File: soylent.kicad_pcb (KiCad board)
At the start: 2 copper layers, 34.5 x 43.2 mm, 23 parts, among them J1 DB9_Female, J2 Conn_01x04, J3 Conn_01x04, J4 Conn_02x03_Counter_Clockwise, Q1 BC847BPN, Q2 BC847BPN, U1 ATtiny202-SS, U2 MIC5504-3.3YM5

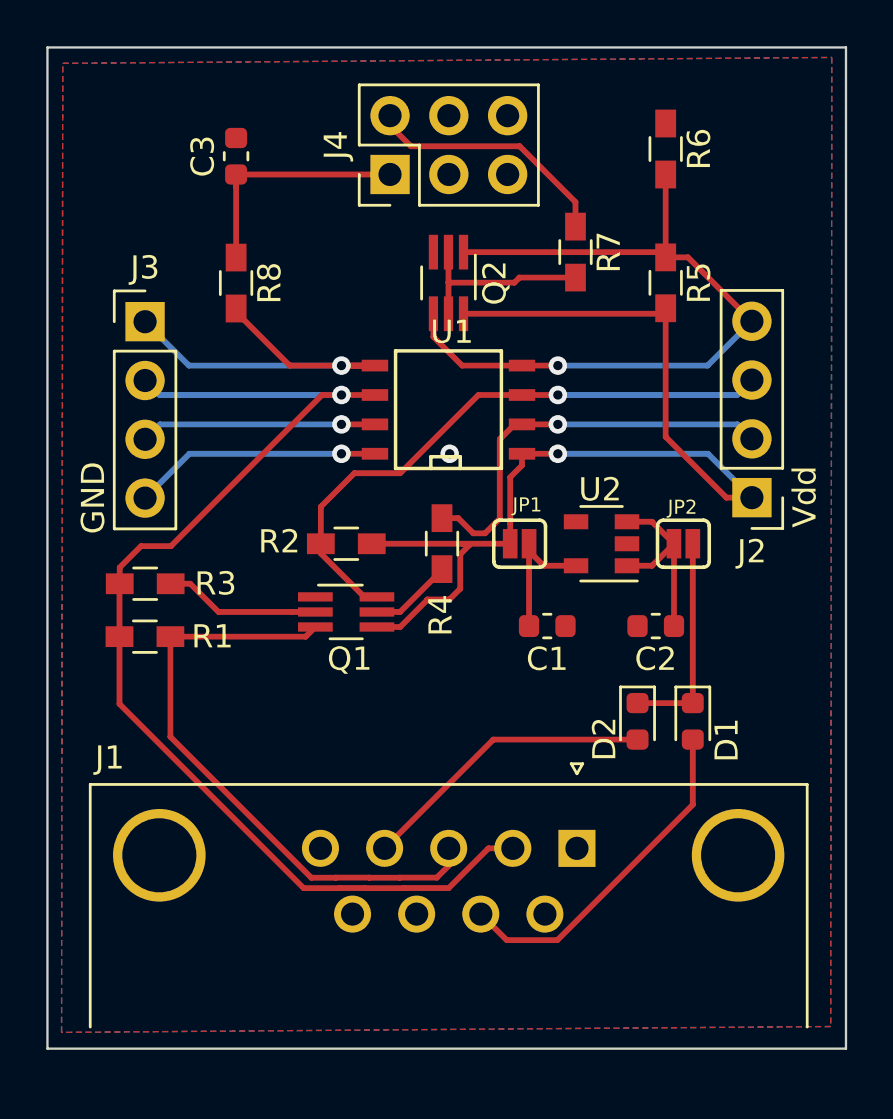
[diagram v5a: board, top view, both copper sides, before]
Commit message: Use hand-soldering footprints more consistently
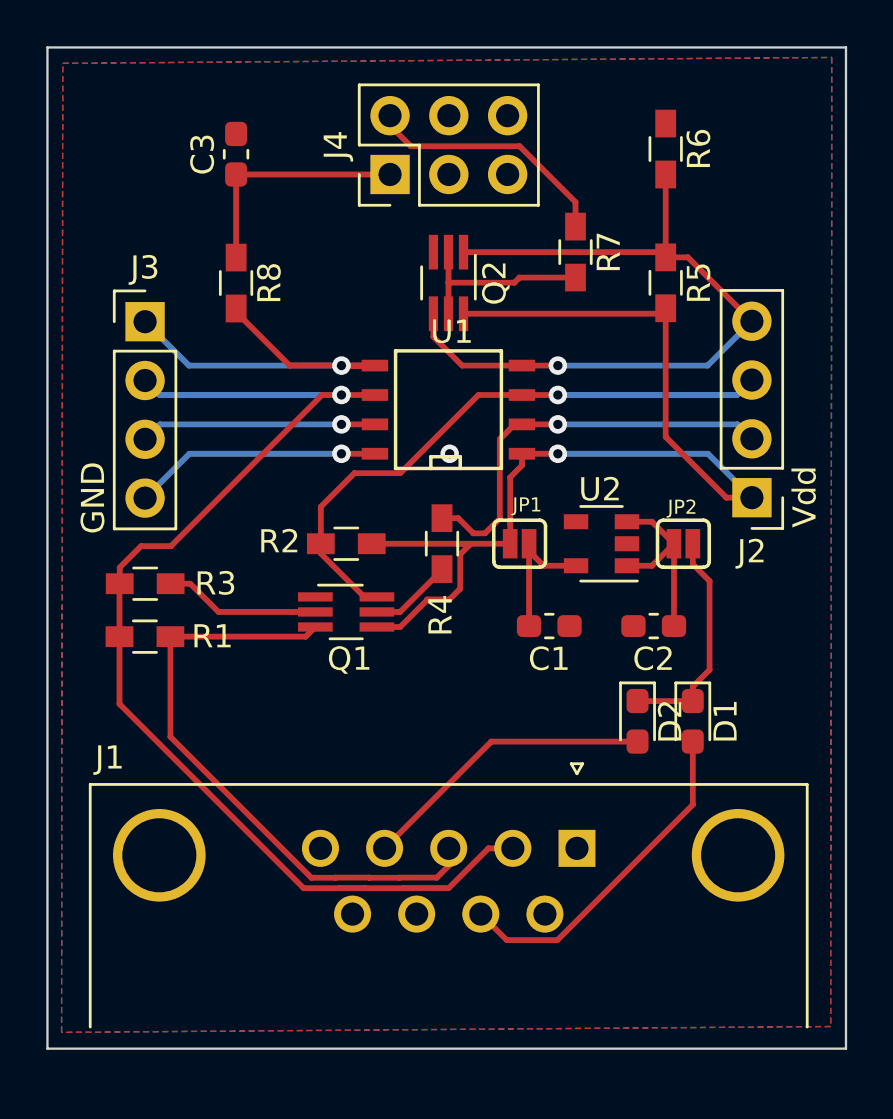
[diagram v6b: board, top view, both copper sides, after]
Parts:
- C1, C2, C3: footprint Capacitor_SMD:C_0603_1608Metric -> Capacitor_SMD:C_0603_1608Metric_Pad1.05x0.95mm_HandSolder
- D1, D2: footprint Diode_SMD:D_0603_1608Metric -> Diode_SMD:D_0603_1608Metric_Pad1.05x0.95mm_HandSolder
- moved C1 0.09 mm to (243.6, 44.8)
- moved C2 0.09 mm to (248.1, 44.8)
- moved C3 0.09 mm to (230.0, 24.4)
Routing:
- net Net-(D1-Pad1): track 9.27 -> 9.78 mm

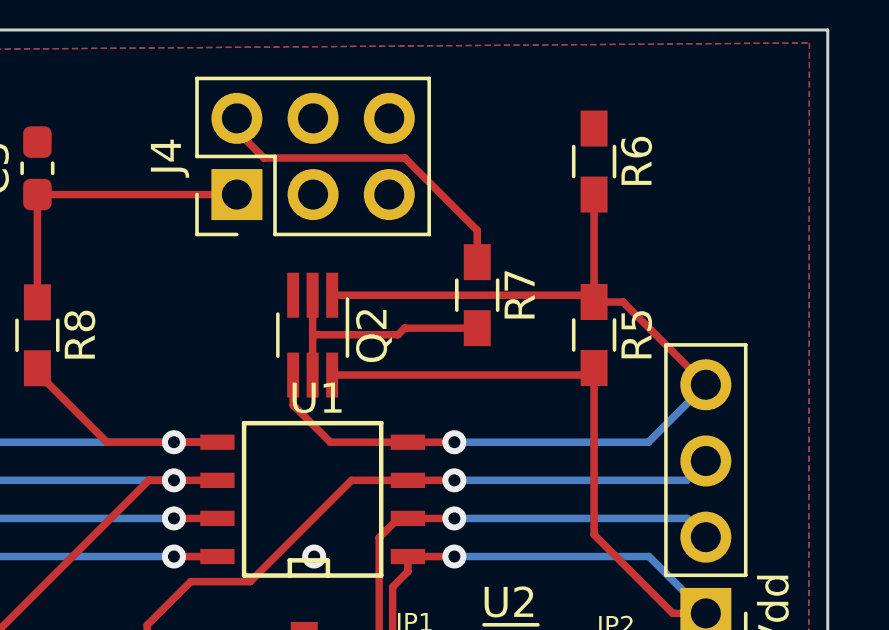
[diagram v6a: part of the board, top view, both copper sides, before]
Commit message: Fix up ground plane fill
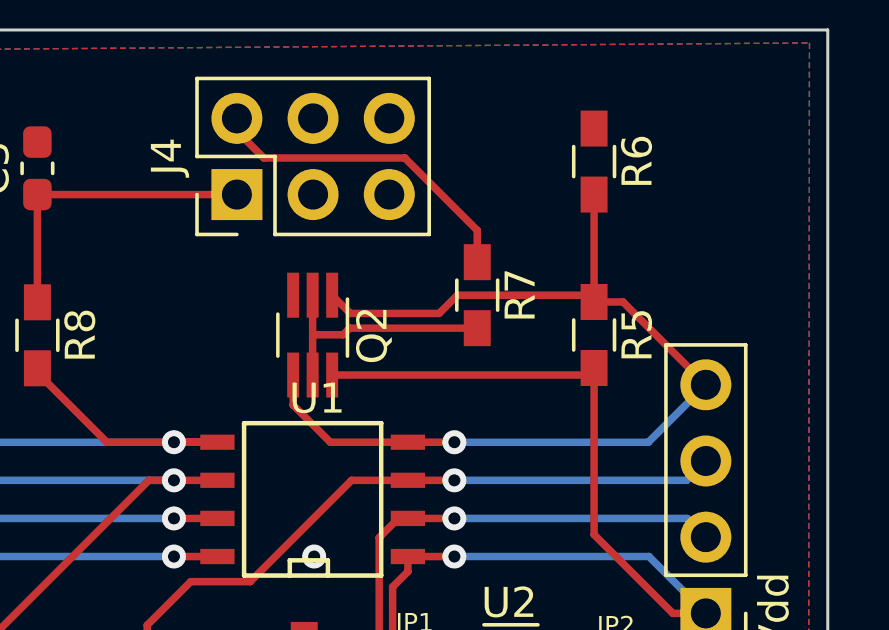
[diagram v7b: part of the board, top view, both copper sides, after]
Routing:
- net /PA1: track 33.5 -> 34.0 mm
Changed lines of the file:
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@@
     (thickness 1.6)
     (drawings 6)
-    (tracks 151)
+    (tracks 154)
     (zones 0)
     (modules 23)
@@
   (segment (start 248.5992 28.8276) (end 248.5992 28.6776) (width 0.25) (layer F.Cu) (net 15))
   (segment (start 248.5992 28.8276) (end 248.5992 25.2476) (width 0.25) (layer F.Cu) (net 15))
-  (segment (start 248.3742 28.6026) (end 248.5992 28.8276) (width 0.25) (layer F.Cu) (net 15))
-  (segment (start 239.8672 28.6026) (end 248.3742 28.6026) (width 0.25) (layer F.Cu) (net 15))
   (segment (start 249.5636 28.8276) (end 252.3236 31.5876) (width 0.25) (layer F.Cu) (net 15))
   (segment (start 248.5992 28.8276) (end 249.5636 28.8276) (width 0.25) (layer F.Cu) (net 15))
+  (segment (start 248.3742 28.6026) (end 248.5992 28.8276) (width 0.25) (layer F.Cu) (net 15))
+  (segment (start 244.041 28.6026) (end 248.3742 28.6026) (width 0.25) (layer F.Cu) (net 15))
+  (segment (start 243.4336 29.21) (end 244.041 28.6026) (width 0.25) (layer F.Cu) (net 15))
+  (segment (start 240.4746 29.21) (end 243.4336 29.21) (width 0.25) (layer F.Cu) (net 15))
+  (segment (start 239.8672 28.6026) (end 240.4746 29.21) (width 0.25) (layer F.Cu) (net 15))
   (segment (start 236.0422 33.5026) (end 234.5944 33.5026) (width 0.25) (layer F.Cu) (net 16))
   (via (at 234.5944 33.5026) (size 0.8) (drill 0.4) (layers F.Cu B.Cu) (net 16))
@@
   (segment (start 239.2172 29.9212) (end 239.2172 28.6026) (width 0.25) (layer F.Cu) (net 18))
   (segment (start 239.2172 31.2626) (end 239.2172 29.9212) (width 0.25) (layer F.Cu) (net 18))
-  (segment (start 242.2828 29.7004) (end 244.7036 29.7004) (width 0.25) (layer F.Cu) (net 18))
-  (segment (start 242.062 29.9212) (end 242.2828 29.7004) (width 0.25) (layer F.Cu) (net 18))
-  (segment (start 239.2172 29.9212) (end 242.062 29.9212) (width 0.25) (layer F.Cu) (net 18))
+  (segment (start 240.454 29.7004) (end 244.7036 29.7004) (width 0.25) (layer F.Cu) (net 18))
+  (segment (start 240.2332 29.9212) (end 240.454 29.7004) (width 0.25) (layer F.Cu) (net 18))
+  (segment (start 239.2172 29.9212) (end 240.2332 29.9212) (width 0.25) (layer F.Cu) (net 18))
   (segment (start 230.0422 25.2476) (end 236.6922 25.2476) (width 0.25) (layer F.Cu) (net 19))
   (segment (start 230.0422 28.8376) (end 230.0422 25.2476) (width 0.25) (layer F.Cu) (net 19))

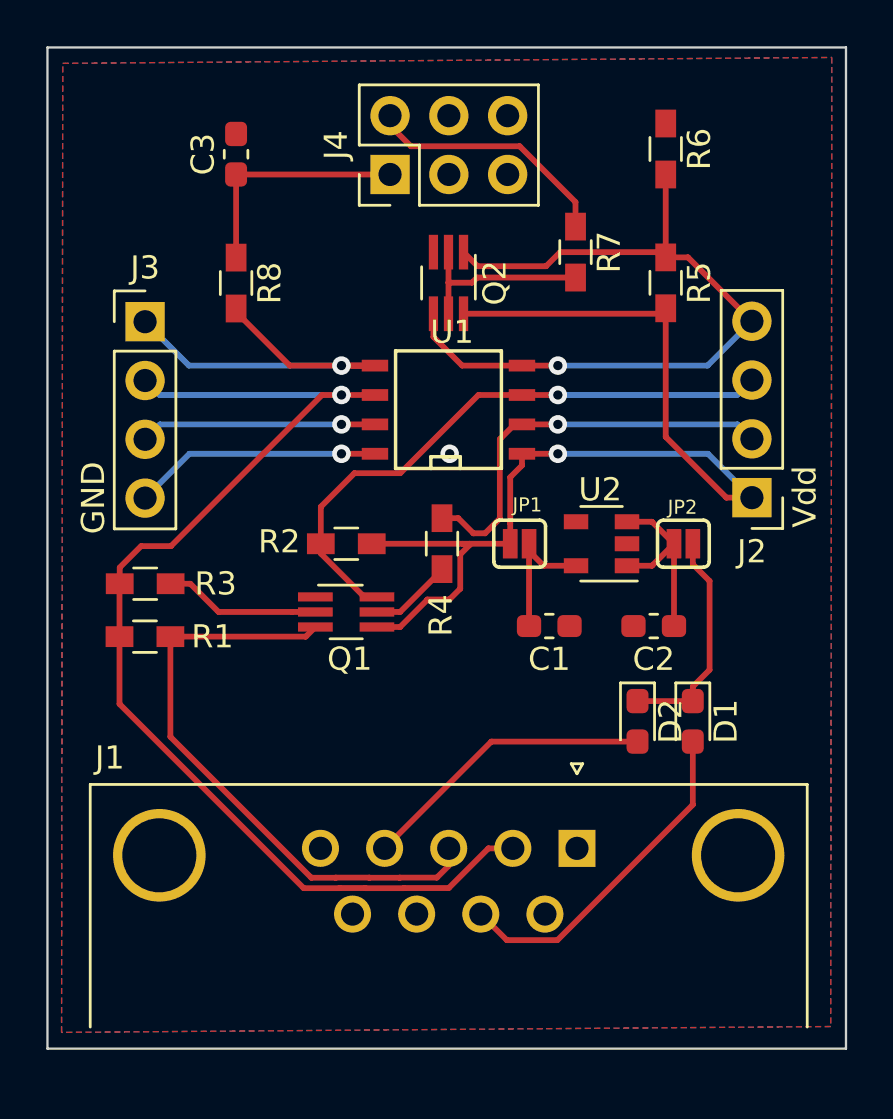
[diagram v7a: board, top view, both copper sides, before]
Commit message: Cosmetic replacement and rerouting
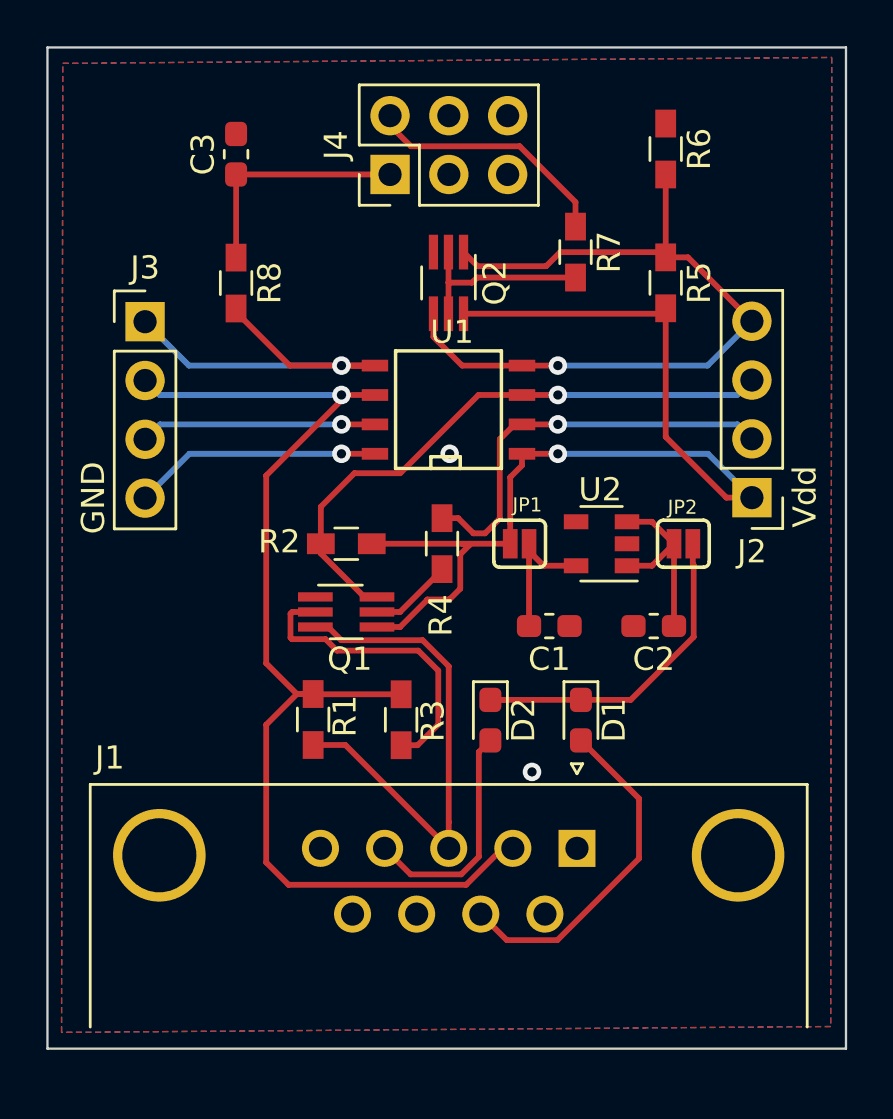
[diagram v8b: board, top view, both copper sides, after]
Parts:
- moved R3 12.5 mm to (237.2, 48.8), turned to 270 degrees
- moved R1 8.10 mm to (233.4, 48.8), turned to 90 degrees
- moved D2 6.36 mm to (241.0, 48.8)
- moved D1 4.83 mm to (244.9, 48.8)
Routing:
- net Net-(Q1-Pad2): track 6.76 -> 13.4 mm
- net /RD: track 26.3 -> 22.0 mm
- net Net-(D1-Pad1): track 9.78 -> 13.9 mm
- net /DTR: track 12.8 -> 10.1 mm
- net GND: vias 2 -> 3
